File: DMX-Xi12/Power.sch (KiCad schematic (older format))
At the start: 20 parts, among them Con11 BARREL_JACK, U3 LTV-354T, U4 7805n, U5 LTV-354T

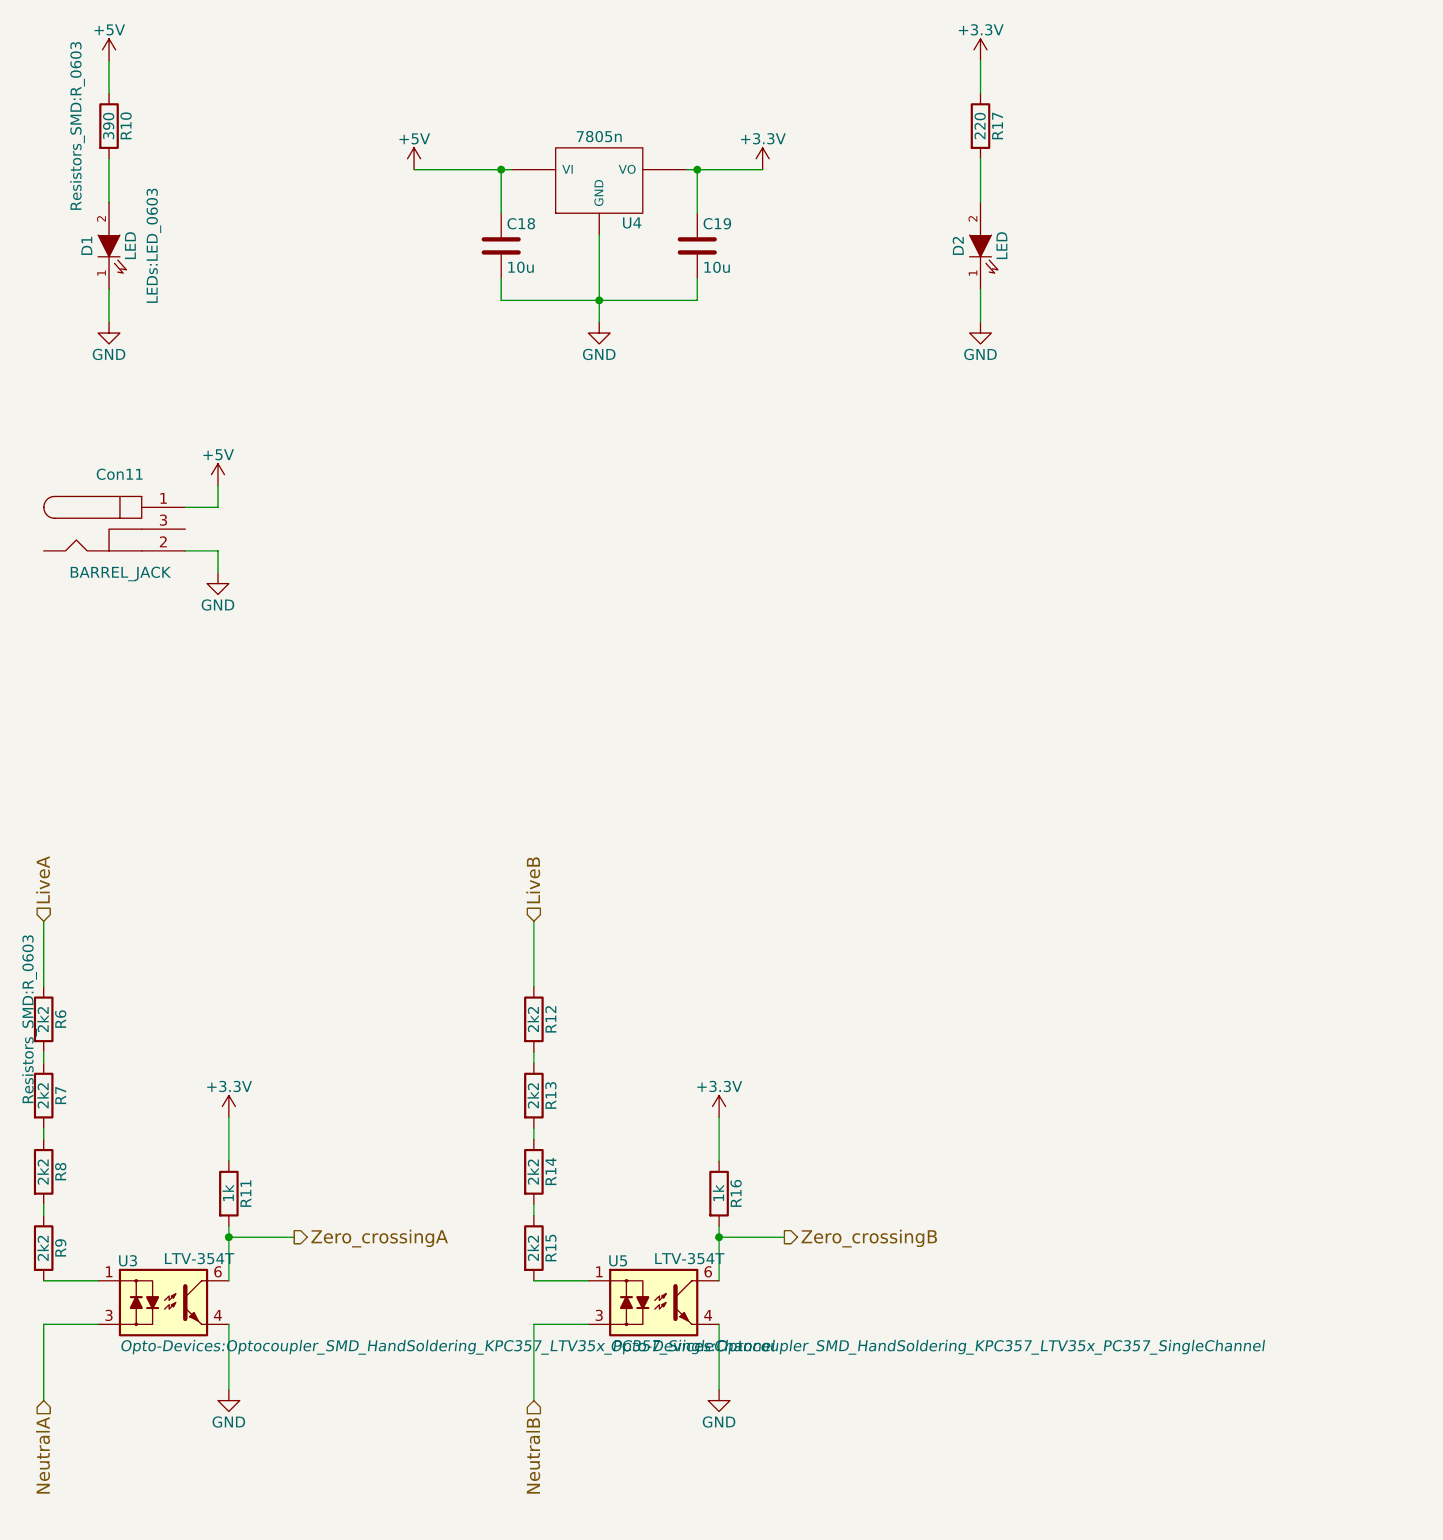
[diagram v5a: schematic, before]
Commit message: completed board. Schematic, is correct but some part values and numbers need updating! Do not trust the schematic yet
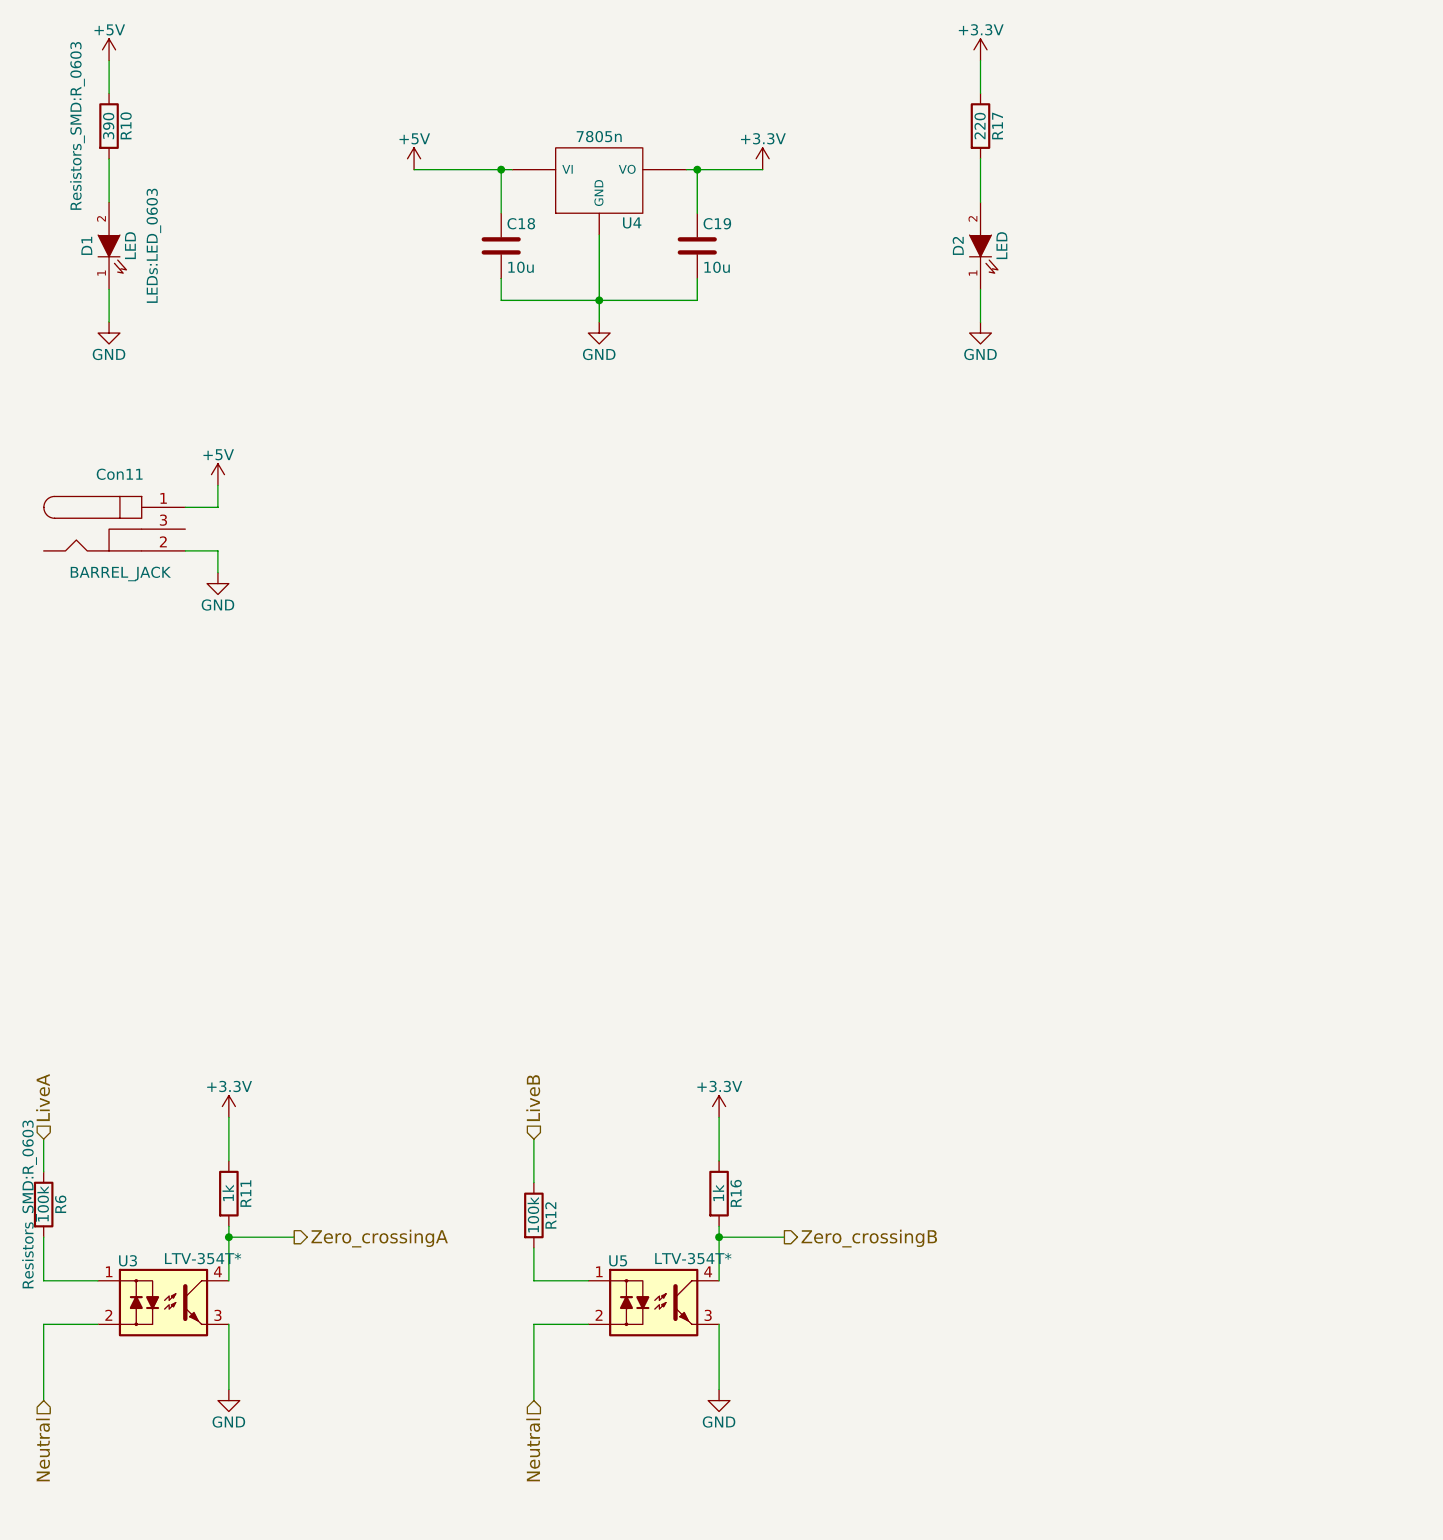
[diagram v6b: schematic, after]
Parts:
- removed R13, R14, R15, R7, R8, R9: 2k2, Resistors_SMD:R_0603, symbol R
- removed U3, U5: LTV-354T, Opto-Devices:Optocoupler_SMD_HandSoldering_KPC357_LTV35x_PC357_SingleChannel, symbol LTV-354T
- added U3, U5: LTV-354T*, symbol LTV-354T*
- R12, R6: value 2k2 -> 100k
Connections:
- net GND: now also U3.3, U5.3
- net Zero_crossingA: now also U3.4
- net Zero_crossingB: now also U5.4
- net at R6.2: now also U3.1
- net at R12.2: now also U5.1
- new net Neutral: U3.2, U5.2
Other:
- moved on the sheet: R12, R6
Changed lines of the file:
@@
 $EndDescr
 $Comp
-L +5V #PWR029
+L +5V #PWR030
 U 1 1 56B6829F
 P 2600 1450
-F 0 "#PWR029" H 2600 1300 50  0001 C CNN
+F 0 "#PWR030" H 2600 1300 50  0001 C CNN
 F 1 "+5V" H 2600 1590 50  0000 C CNN
 F 2 "" H 2600 1450 50  0000 C CNN
@@
 $EndComp
 $Comp
-L GND #PWR030
+L GND #PWR031
 U 1 1 56B682B8
 P 3450 2150
-F 0 "#PWR030" H 3450 1900 50  0001 C CNN
+F 0 "#PWR031" H 3450 1900 50  0001 C CNN
 F 1 "GND" H 3450 2000 50  0000 C CNN
 F 2 "" H 3450 2150 50  0000 C CNN
@@
 $EndComp
 $Comp
-L +3.3V #PWR031
+L +3.3V #PWR032
 U 1 1 56B6835A
 P 4200 1450
-F 0 "#PWR031" H 4200 1300 50  0001 C CNN
+F 0 "#PWR032" H 4200 1300 50  0001 C CNN
 F 1 "+3.3V" H 4200 1590 50  0000 C CNN
 F 2 "" H 4200 1450 50  0000 C CNN
@@
 $EndComp
 $Comp
-L +5V #PWR032
+L +5V #PWR033
 U 1 1 56CBF4F1
 P 1200 950
-F 0 "#PWR032" H 1200 800 50  0001 C CNN
+F 0 "#PWR033" H 1200 800 50  0001 C CNN
 F 1 "+5V" H 1200 1090 50  0000 C CNN
 F 2 "" H 1200 950 50  0000 C CNN
@@
 $EndComp
 $Comp
-L GND #PWR033
+L GND #PWR034
 U 1 1 56CBF50D
 P 1200 2150
-F 0 "#PWR033" H 1200 1900 50  0001 C CNN
+F 0 "#PWR034" H 1200 1900 50  0001 C CNN
 F 1 "GND" H 1200 2000 50  0000 C CNN
 F 2 "" H 1200 2150 50  0000 C CNN
@@
 $EndComp
 $Comp
-L GND #PWR034
+L GND #PWR035
 U 1 1 56CBF934
 P 5200 2150
-F 0 "#PWR034" H 5200 1900 50  0001 C CNN
+F 0 "#PWR035" H 5200 1900 50  0001 C CNN
 F 1 "GND" H 5200 2000 50  0000 C CNN
 F 2 "" H 5200 2150 50  0000 C CNN
@@
 $EndComp
 $Comp
-L +3.3V #PWR035
+L +3.3V #PWR036
 U 1 1 56CBF969
 P 5200 950
-F 0 "#PWR035" H 5200 800 50  0001 C CNN
+F 0 "#PWR036" H 5200 800 50  0001 C CNN
 F 1 "+3.3V" H 5200 1090 50  0000 C CNN
 F 2 "" H 5200 950 50  0000 C CNN
 F 3 "" H 5200 950 50  0000 C CNN
 	1    5200 950
-	1    0    0    -1
-$EndComp
-$Comp
-L LTV-354T U3
-U 1 1 56CCBACF
-P 1450 6650
-F 0 "U3" H 1240 6840 50  0000 L CNN
-F 1 "LTV-354T" H 1450 6850 50  0000 L CNN
-F 2 "Opto-Devices:Optocoupler_SMD_HandSoldering_KPC357_LTV35x_PC357_SingleChannel" H 1250 6450 50  0000 L CIN
-F 3 "" H 1475 6650 50  0000 L CNN
-	1    1450 6650
 	1    0    0    -1
 $EndComp
@@
 $EndComp
 $Comp
-L GND #PWR036
+L GND #PWR037
 U 1 1 56CCC098
 P 1750 7050
-F 0 "#PWR036" H 1750 6800 50  0001 C CNN
+F 0 "#PWR037" H 1750 6800 50  0001 C CNN
 F 1 "GND" H 1750 6900 50  0000 C CNN
 F 2 "" H 1750 7050 50  0000 C CNN
@@
 	1    0    0    -1
 $EndComp
-$Comp
-L R R9
-U 1 1 56CCC1C9
-P 900 6400
-F 0 "R9" V 980 6400 50  0000 C CNN
-F 1 "2k2" V 900 6400 50  0000 C CNN
-F 2 "Resistors_SMD:R_0603" V 830 6400 50  0001 C CNN
-F 3 "" H 900 6400 50  0000 C CNN
-	1    900  6400
-	1    0    0    -1
-$EndComp
-$Comp
-L R R8
-U 1 1 56CCC234
-P 900 6050
-F 0 "R8" V 980 6050 50  0000 C CNN
-F 1 "2k2" V 900 6050 50  0000 C CNN
-F 2 "Resistors_SMD:R_0603" V 830 6050 50  0001 C CNN
-F 3 "" H 900 6050 50  0000 C CNN
-	1    900  6050
-	1    0    0    -1
-$EndComp
-$Comp
-L R R7
-U 1 1 56CCC289
-P 900 5700
-F 0 "R7" V 980 5700 50  0000 C CNN
-F 1 "2k2" V 900 5700 50  0000 C CNN
-F 2 "Resistors_SMD:R_0603" V 830 5700 50  0001 C CNN
-F 3 "" H 900 5700 50  0000 C CNN
-	1    900  5700
-	1    0    0    -1
-$EndComp
 Wire Wire Line
 	2600 1450 3050 1450
@@
 Wire Wire Line
 	1150 6550 900  6550
-Wire Wire Line
-	900  5850 900  5900
-Wire Wire Line
-	900  6200 900  6250
 Text HLabel 2050 6350 2    60   Output ~ 0
 Zero_crossingA
@@
 L R R6
 U 1 1 56D29409
-P 900 5350
-F 0 "R6" V 980 5350 50  0000 C CNN
-F 1 "2k2" V 900 5350 50  0000 C CNN
-F 2 "Resistors_SMD:R_0603" V 830 5350 50  0000 C CNN
-F 3 "" H 900 5350 50  0000 C CNN
-	1    900  5350
-	1    0    0    -1
-$EndComp
-Wire Wire Line
-	900  5500 900  5550
-Wire Wire Line
-	900  4900 900  5200
-$Comp
-L LTV-354T U5
-U 1 1 56D2988E
-P 3700 6650
-F 0 "U5" H 3490 6840 50  0000 L CNN
-F 1 "LTV-354T" H 3700 6850 50  0000 L CNN
-F 2 "Opto-Devices:Optocoupler_SMD_HandSoldering_KPC357_LTV35x_PC357_SingleChannel" H 3500 6450 50  0000 L CIN
-F 3 "" H 3725 6650 50  0000 L CNN
-	1    3700 6650
+P 900 6200
+F 0 "R6" V 980 6200 50  0000 C CNN
+F 1 "100k" V 900 6200 50  0000 C CNN
+F 2 "Resistors_SMD:R_0603" V 830 6200 50  0000 C CNN
+F 3 "" H 900 6200 50  0000 C CNN
+	1    900  6200
 	1    0    0    -1
 $EndComp
@@
 $EndComp
 $Comp
-L GND #PWR037
+L GND #PWR038
 U 1 1 56D298A6
 P 4000 7050
-F 0 "#PWR037" H 4000 6800 50  0001 C CNN
+F 0 "#PWR038" H 4000 6800 50  0001 C CNN
 F 1 "GND" H 4000 6900 50  0000 C CNN
 F 2 "" H 4000 7050 50  0000 C CNN
@@
 	1    0    0    -1
 $EndComp
-$Comp
-L R R15
-U 1 1 56D298AC
-P 3150 6400
-F 0 "R15" V 3230 6400 50  0000 C CNN
-F 1 "2k2" V 3150 6400 50  0000 C CNN
-F 2 "Resistors_SMD:R_0603" V 3080 6400 50  0001 C CNN
-F 3 "" H 3150 6400 50  0000 C CNN
-	1    3150 6400
-	1    0    0    -1
-$EndComp
-$Comp
-L R R14
-U 1 1 56D298B2
-P 3150 6050
-F 0 "R14" V 3230 6050 50  0000 C CNN
-F 1 "2k2" V 3150 6050 50  0000 C CNN
-F 2 "Resistors_SMD:R_0603" V 3080 6050 50  0001 C CNN
-F 3 "" H 3150 6050 50  0000 C CNN
-	1    3150 6050
-	1    0    0    -1
-$EndComp
-$Comp
-L R R13
-U 1 1 56D298B8
-P 3150 5700
-F 0 "R13" V 3230 5700 50  0000 C CNN
-F 1 "2k2" V 3150 5700 50  0000 C CNN
-F 2 "Resistors_SMD:R_0603" V 3080 5700 50  0001 C CNN
-F 3 "" H 3150 5700 50  0000 C CNN
-	1    3150 5700
-	1    0    0    -1
-$EndComp
 Wire Wire Line
 	4000 5800 4000 6000
@@
 Wire Wire Line
 	3400 6550 3150 6550
-Wire Wire Line
-	3150 5850 3150 5900
-Wire Wire Line
-	3150 6200 3150 6250
 Text HLabel 4300 6350 2    60   Output ~ 0
 Zero_crossingB
@@
 	4300 6350 4000 6350
 Connection ~ 4000 6350
-$Comp
-L R R12
-U 1 1 56D298CF
-P 3150 5350
-F 0 "R12" V 3230 5350 50  0000 C CNN
-F 1 "2k2" V 3150 5350 50  0000 C CNN
-F 2 "Resistors_SMD:R_0603" V 3080 5350 50  0001 C CNN
-F 3 "" H 3150 5350 50  0000 C CNN
-	1    3150 5350
-	1    0    0    -1
-$EndComp
-Wire Wire Line
-	3150 5500 3150 5550
-Wire Wire Line
-	3150 4900 3150 5200
-Text HLabel 900  4900 1    60   Input ~ 0
+Text HLabel 900  5900 1    60   Input ~ 0
 LiveA
-Text HLabel 3150 4900 1    60   Input ~ 0
+Text HLabel 3150 5900 1    60   Input ~ 0
 LiveB
 $Comp
-L +3.3V #PWR038
+L +3.3V #PWR039
 U 1 1 56D2A01A
 P 1750 5800
-F 0 "#PWR038" H 1750 5650 50  0001 C CNN
+F 0 "#PWR039" H 1750 5650 50  0001 C CNN
 F 1 "+3.3V" H 1750 5940 50  0000 C CNN
 F 2 "" H 1750 5800 50  0000 C CNN
@@
 $EndComp
 $Comp
-L +3.3V #PWR039
+L +3.3V #PWR040
 U 1 1 56D2A058
 P 4000 5800
-F 0 "#PWR039" H 4000 5650 50  0001 C CNN
+F 0 "#PWR040" H 4000 5650 50  0001 C CNN
 F 1 "+3.3V" H 4000 5940 50  0000 C CNN
 F 2 "" H 4000 5800 50  0000 C CNN
@@
 $EndComp
 Text HLabel 900  7100 3    60   Input ~ 0
-NeutralA
-Text HLabel 3150 7100 3    60   Input ~ 0
-NeutralB
+Neutral
 $Comp
 L BARREL_JACK Con11
@@
 $EndComp
 $Comp
-L +5V #PWR040
+L +5V #PWR041
 U 1 1 5702E5CD
 P 1700 2900
-F 0 "#PWR040" H 1700 2750 50  0001 C CNN
+F 0 "#PWR041" H 1700 2750 50  0001 C CNN
 F 1 "+5V" H 1700 3040 50  0000 C CNN
 F 2 "" H 1700 2900 50  0000 C CNN
@@
 	1700 3000 1550 3000
 $Comp
-L GND #PWR041
+L GND #PWR042
 U 1 1 5702E648
 P 1700 3300
-F 0 "#PWR041" H 1700 3050 50  0001 C CNN
+F 0 "#PWR042" H 1700 3050 50  0001 C CNN
 F 1 "GND" H 1700 3150 50  0000 C CNN
 F 2 "" H 1700 3300 50  0000 C CNN
@@
 F 0 "U4" H 3600 1304 50  0000 C CNN
 F 1 "7805n" H 3450 1700 50  0000 C CNN
-F 2 "" H 3450 1500 50  0000 C CNN
+F 2 "" H 3450 1500 50  0001 C CNN
 F 3 "" H 3450 1500 50  0000 C CNN
 	1    3450 1500
 	1    0    0    -1
 $EndComp
+$Comp
+L LTV-354T* U3
+U 1 1 5711EAA7
+P 1450 6650
+F 0 "U3" H 1240 6840 50  0000 L CNN
+F 1 "LTV-354T*" H 1450 6850 50  0000 L CNN
+F 2 "" H 1250 6450 50  0001 L CIN
+F 3 "" H 1475 6650 50  0000 L CNN
+	1    1450 6650
+	1    0    0    -1
+$EndComp
+$Comp
+L LTV-354T* U5
+U 1 1 5711EE63
+P 3700 6650
+F 0 "U5" H 3490 6840 50  0000 L CNN
+F 1 "LTV-354T*" H 3700 6850 50  0000 L CNN
+F 2 "" H 3500 6450 50  0001 L CIN
+F 3 "" H 3725 6650 50  0000 L CNN
+	1    3700 6650
+	1    0    0    -1
+$EndComp
+Text HLabel 3150 7100 3    60   Input ~ 0
+Neutral
+$Comp
+L R R12
+U 1 1 56D298CF
+P 3150 6250
+F 0 "R12" V 3230 6250 50  0000 C CNN
+F 1 "100k" V 3150 6250 50  0000 C CNN
+F 2 "Resistors_SMD:R_0603" V 3080 6250 50  0001 C CNN
+F 3 "" H 3150 6250 50  0000 C CNN
+	1    3150 6250
+	1    0    0    -1
+$EndComp
+Wire Wire Line
+	3150 5900 3150 6100
+Wire Wire Line
+	3150 6550 3150 6400
+Wire Wire Line
+	900  6050 900  5900
+Wire Wire Line
+	900  6550 900  6350
 $EndSCHEMATC
